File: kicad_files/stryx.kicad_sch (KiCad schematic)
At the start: 27 parts, among them J1 USB_B_Micro, M1 12V 250 RPM, M2 12V 250 RPM, SW1 SW_SPDT, U1 LM317_TO-220, U2 NUCLEO-L432KC, U3 TB6612FNG-Module, U4 HC-SR04, U5 NRF24L01_Breakout

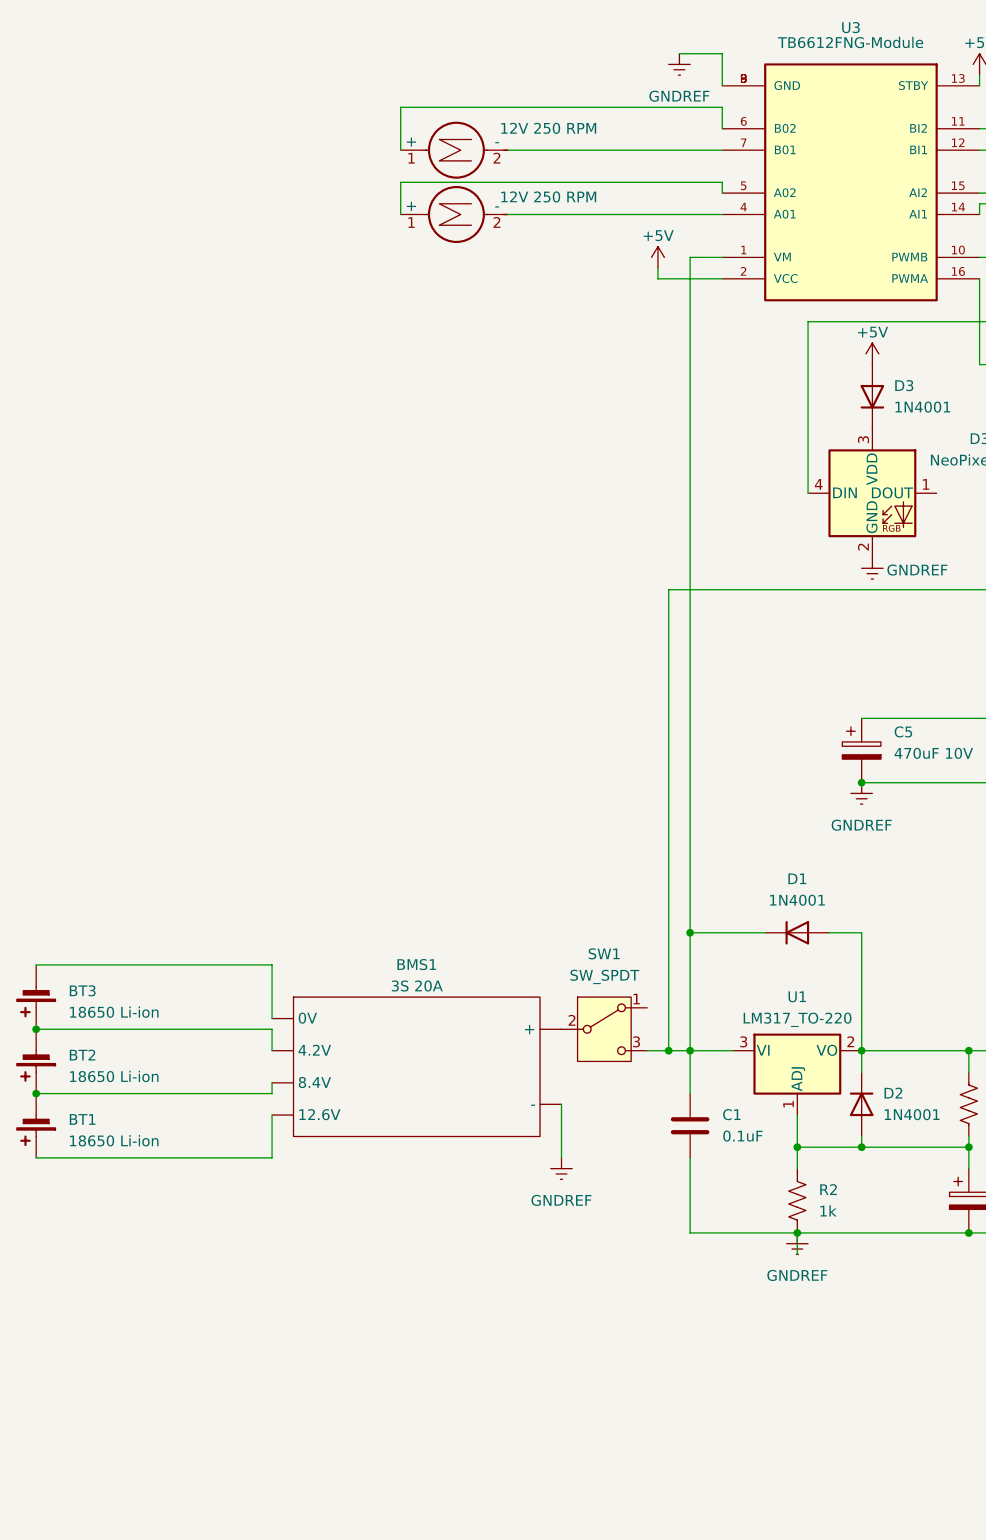
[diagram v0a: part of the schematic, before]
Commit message: Switched to screw terminals in the schematic and added their footprints
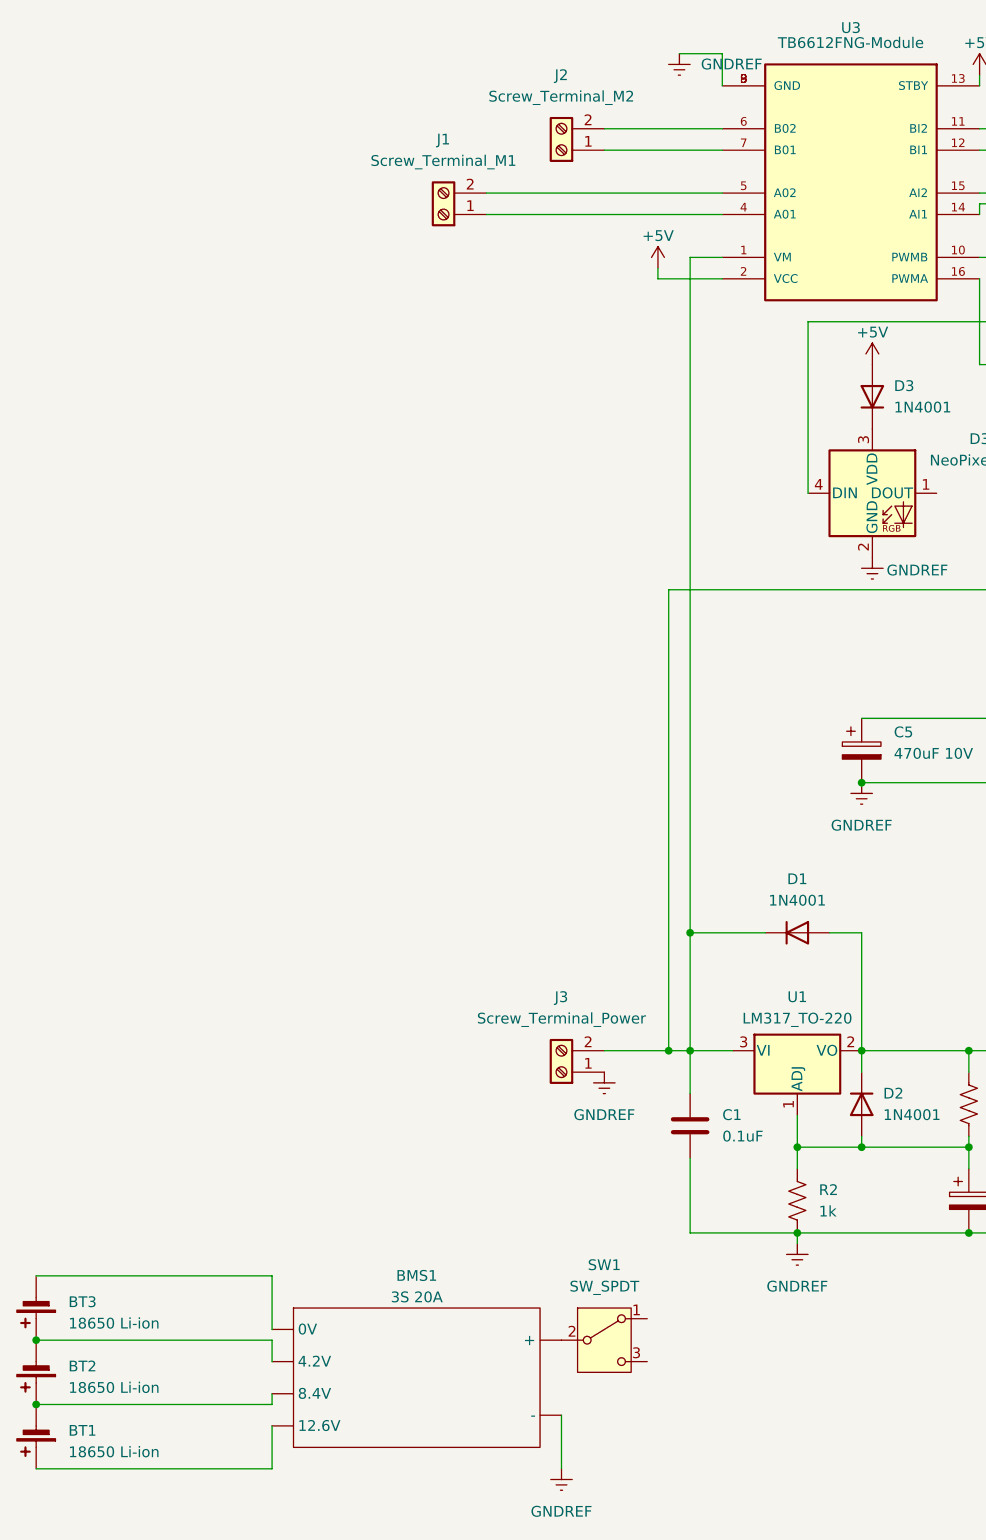
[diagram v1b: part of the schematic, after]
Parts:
- removed M1, M2: 12V 250 RPM, symbol Motor:Motor_DC
- added J1: Screw_Terminal_M1, TerminalBlock_MetzConnect:TerminalBlock_MetzConnect_Type703_RT10N02HGLU_1x02_P9.52mm_Horizontal, symbol Connector:Screw_Terminal_01x02
- added J2: Screw_Terminal_M2, TerminalBlock_MetzConnect:TerminalBlock_MetzConnect_Type703_RT10N02HGLU_1x02_P9.52mm_Horizontal, symbol Connector:Screw_Terminal_01x02
- added J3: Screw_Terminal_Power, TerminalBlock_MetzConnect:TerminalBlock_MetzConnect_Type703_RT10N02HGLU_1x02_P9.52mm_Horizontal, symbol Connector:Screw_Terminal_01x02
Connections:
- net GNDREF: now also J3.1 (Pin_1)
- net at C1.2, D1.1 (K), R3.1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: now also J3.2 (Pin_2); no longer SW1.3 (C)
- net at U3.4 (A01): now also J1.1 (Pin_1)
- net at U3.5 (A02): now also J1.2 (Pin_2)
- net at U3.6 (B02): now also J2.2 (Pin_2)
- net at U3.7 (B01): now also J2.1 (Pin_1)
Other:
- moved on the sheet: BMS1, BT1, BT2, BT3, SW1

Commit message: Updated kicad schematic
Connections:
- net GNDREF: now also C6.1; no longer C6.2
- net Neopixel_Din: now reaches D3.4 (DIN), U2.CN3_12 (PA8)
- net 6.8V: now reaches C3.1, C4.1, C5.1, D1.2 (A), D2.1 (K), R1.1, U1.2 (VO), U2.CN4_1 (VIN)
- net Vbat_Sense: now reaches R3.2, R4.1, U2.CN4_8 (PA5)
- net Vbat_Sense: now also C6.2; no longer C6.1
- net Vbat: now reaches C1.2, D1.1 (K), J3.2 (Pin_2), R3.1, U1.3 (VI), U3.1 (VM)
- net Vbat: now also SW1.3 (C)
- net PWM_M2: now reaches U2.CN3_1 (PA9), U3.10 (PWMB)
- net Dir2_M2: now reaches U2.CN3_7 (PB7), U3.11 (BI2)
- net Dir1_M2: now reaches U2.CN3_8 (PB6), U3.12 (BI1)
- net Dir1_M1: now reaches U2.CN3_6 (PB0), U3.14 (AI1)
- net Dir2_M1: now reaches U2.CN3_9 (PB1), U3.15 (AI2)
- net PWM_M1: now reaches U2.CN3_2 (PA10), U3.16 (PWMA)
- net Sonar_TRIG: now reaches U2.CN4_5 (PA2), U4.2 (TRIG)
- net Sonar_ECHO: now reaches U2.CN4_12 (PA0), U4.3 (ECHO)
- net USB_D-: now reaches J1.2 (D-), U2.CN3_13 (PA11)
- net USB_D+: now reaches J1.3 (D+), U2.CN3_5 (PA12)
- net Wireless_MOSI: now reaches U2.CN3_14 (PB5), U5.6 (MOSI)
- net Wireless_MISO: now reaches U2.CN3_15 (PB4), U5.7 (MISO)
- net Wireless_CSNB: now reaches U2.CN4_10 (PA3), U5.4 (~{CSN})
- net Wireless_IRQ: now reaches U2.CN4_11 (PA1), U5.8 (IRQ)
- net Wireless_SCK: now reaches U2.CN4_15 (PB3), U5.5 (SCK)
- net Wireless_CE: now reaches U2.CN4_9 (PA4), U5.3 (CE)
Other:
- note added: "Battery Input"
- note added: "Battery Level Indication"
- note added: "Battery Voltage Sensing"
- note added: "MCU-CN3"
- note added: "MCU-CN4"
- note added: "Motor Driver"
- note added: "USB"
- note added: "Ultrasonic Sensor"
- note added: "Voltage Regulation"
- note added: "Wireless Communication"
- note removed: "6.8V"
- moved on the sheet: BMS1, BT1, BT2, BT3, C1, C2, C3, C4, C5, C6, D1, D2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

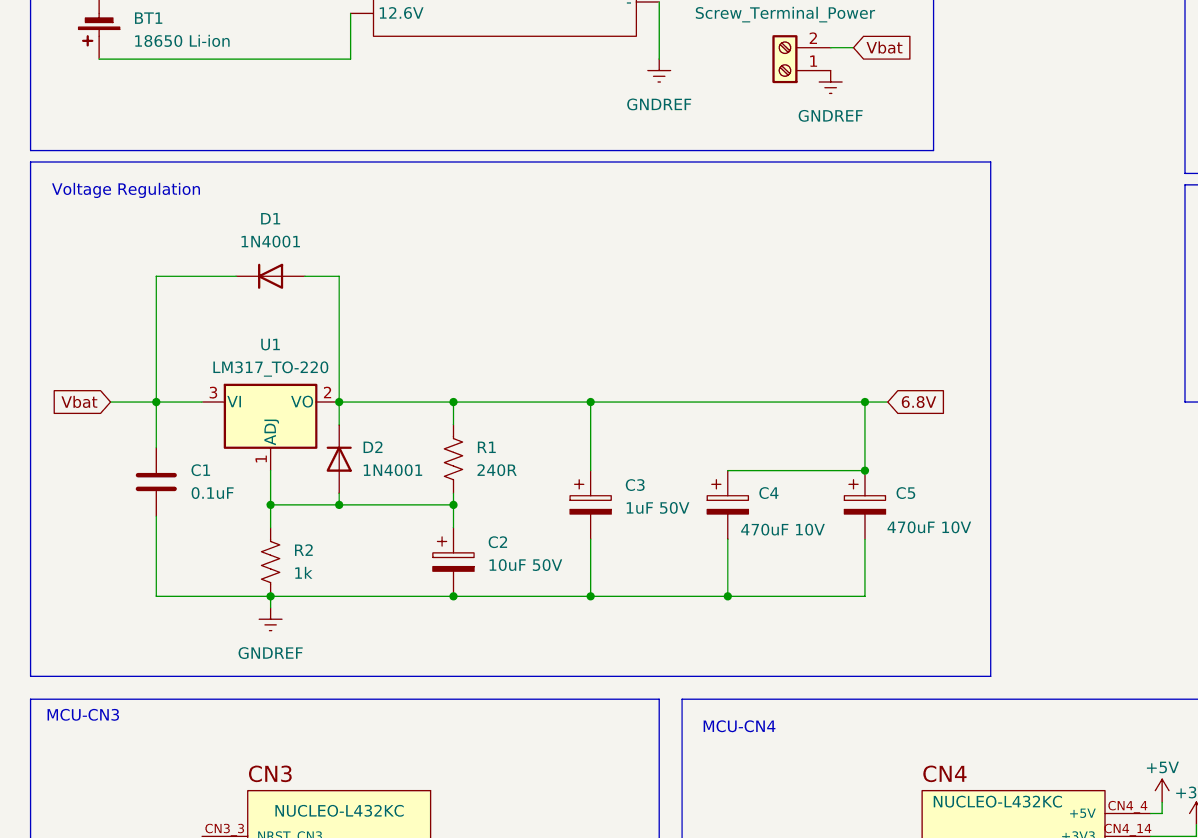
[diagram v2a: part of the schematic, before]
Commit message: Added a schottky diode for reverse polarity protection
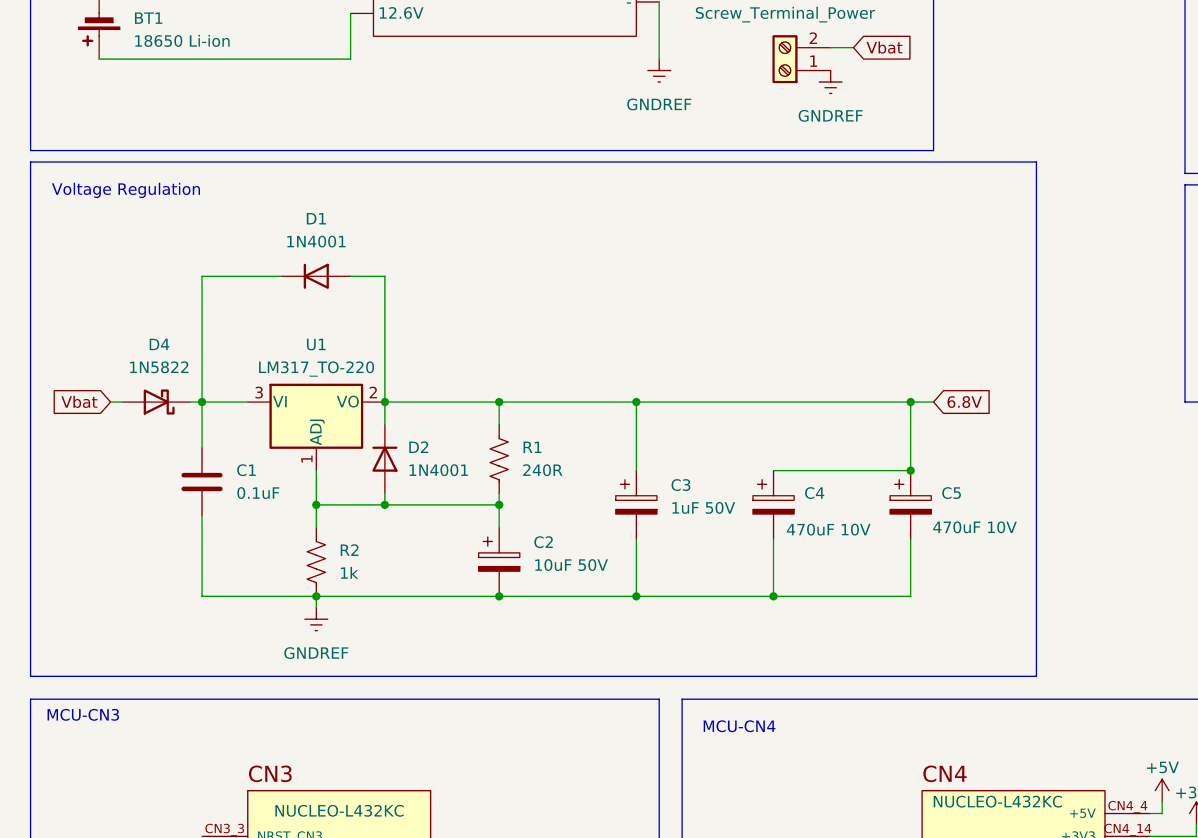
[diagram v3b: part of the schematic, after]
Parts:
- added D4: 1N5822, Diode_THT:D_DO-201AD_P15.24mm_Horizontal, symbol Diode:1N5822
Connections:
- net Vbat: now also D4.2 (A); no longer C1.2, D1.1 (K), U1.3 (VI)
- new net: C1.2, D1.1 (K), D4.1 (K), U1.3 (VI)
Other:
- moved on the sheet: C1, C2, C3, C4, C5, D1, D2, R1, R2, U1
